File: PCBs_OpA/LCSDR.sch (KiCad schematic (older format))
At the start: 5 parts, among them J12 Conn_01x01, J13 Conn_01x01, J14 Conn_01x01, J15 Conn_01x01, J6 I2C

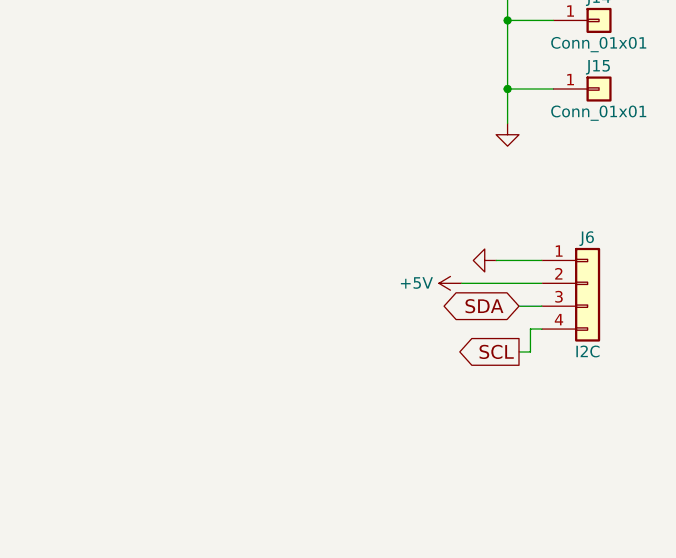
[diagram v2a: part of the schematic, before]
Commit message: Arduino Nano PCB ADX988 DSP
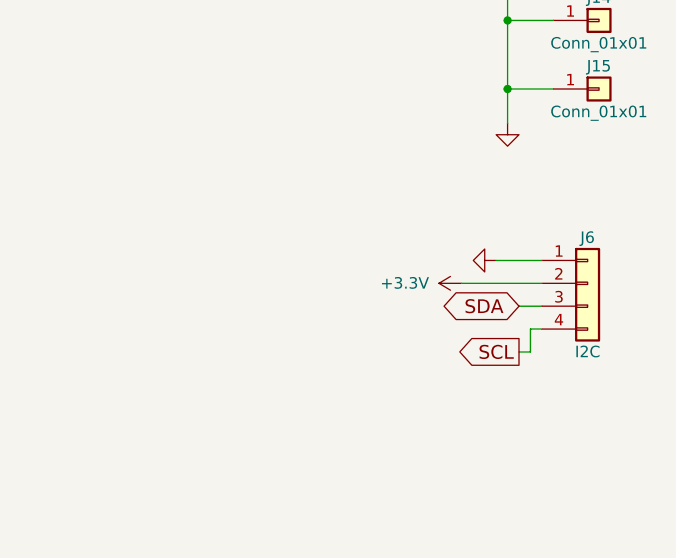
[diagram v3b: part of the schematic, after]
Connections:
- net +5V renamed +3V3
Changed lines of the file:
@@
 LIBS:BF998
 LIBS:relays
+LIBS:MCU_Microchip_ATtiny
 LIBS:LCSDR-cache
 EELAYER 25 0
@@
 	1    8600 3200
 	0    1    1    0
-$EndComp
-$Comp
-L +5V #PWR02
-U 1 1 5FFE0CB0
-P 8450 3300
-F 0 "#PWR02" H 8450 3150 50  0001 C CNN
-F 1 "+5V" V 8450 3500 50  0000 C CNN
-F 2 "" H 8450 3300 50  0001 C CNN
-F 3 "" H 8450 3300 50  0001 C CNN
-	1    8450 3300
-	0    -1   -1   0
 $EndComp
 Wire Wire Line
@@
 F1 "HPF.sch" 60
 $EndSheet
+$Comp
+L +3.3V #PWR?
+U 1 1 63AB3A1B
+P 8450 3300
+F 0 "#PWR?" H 8450 3150 50  0001 C CNN
+F 1 "+3.3V" V 8450 3550 50  0000 C CNN
+F 2 "" H 8450 3300 50  0001 C CNN
+F 3 "" H 8450 3300 50  0001 C CNN
+	1    8450 3300
+	0    -1   -1   0
+$EndComp
 $EndSCHEMATC
